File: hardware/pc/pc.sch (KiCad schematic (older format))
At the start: 126 parts, among them J1 Conn_Power, J2 Conn_PC, U1 74HC161, U10 74HC597, U11 74HC595, U12 74HC161, U13 74HC161, U14 74HC597, U15 74HC595, U16 74HC161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

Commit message: Added test points
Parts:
- added TP1: TestPoint, TestPoint:TestPoint_THTPad_D2.0mm_Drill1.0mm, symbol Connector:TestPoint
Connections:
- net GND: now also TP1.1

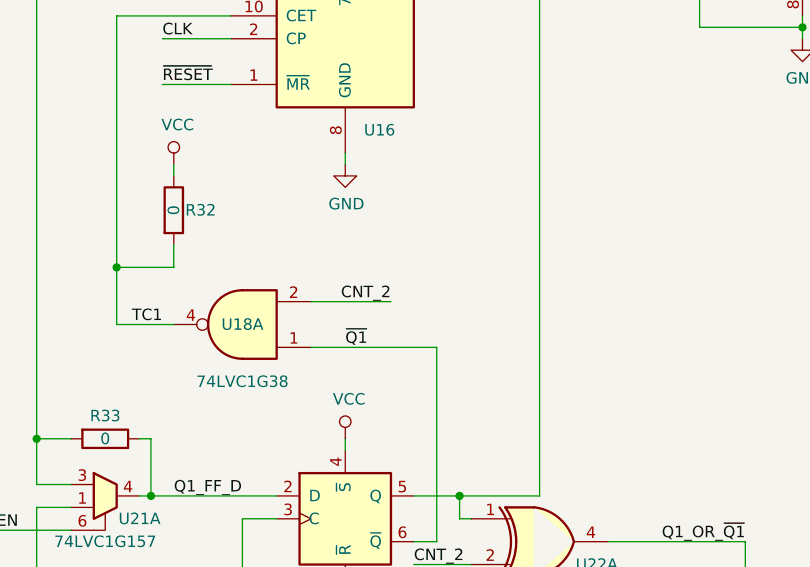
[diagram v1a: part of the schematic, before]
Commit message: Added errata to pc schematic
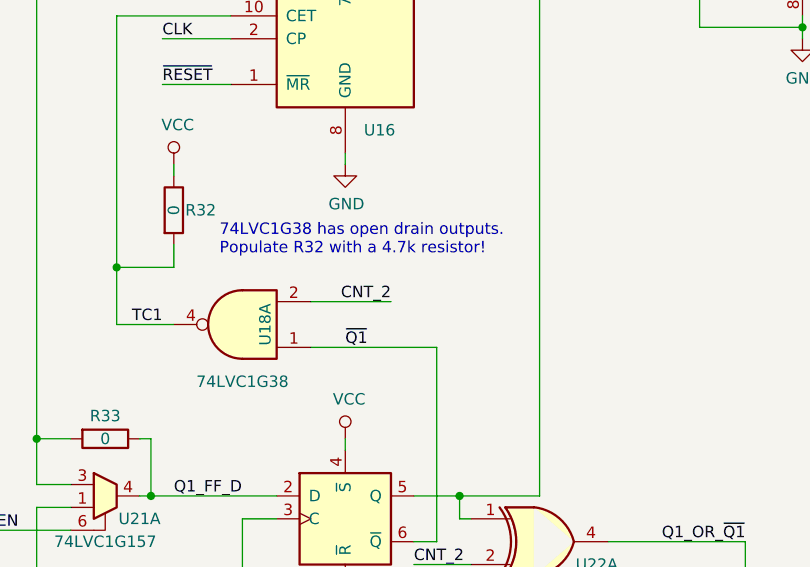
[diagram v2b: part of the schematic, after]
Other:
- note added: "74LVC1G38 has open drain outputs.\nPopulate R32 with a 4.7k resistor!"
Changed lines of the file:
@@
 EESchema Schematic File Version 4
-LIBS:pc-cache
-EELAYER 26 0
+EELAYER 30 0
 EELAYER END
 $Descr A2 16535 23386 portrait
@@
 U 1 1 5F0A6688
 P 6350 19550
-F 0 "U18" H 6350 19550 50  0000 C CNN
+F 0 "U18" V 6250 19550 50  0000 C CNN
 F 1 "74LVC1G38" H 6350 19800 50  0000 C CNN
 F 2 "Package_TO_SOT_SMD:SOT-23-5_HandSoldering" H 6350 19600 50  0001 C CNN
@@
 Wire Wire Line
 	11550 3050 11550 3150
+Text Notes 6250 19250 0    50   ~ 0
+74LVC1G38 has open drain outputs.\nPopulate R32 with a 4.7k resistor!
 $EndSCHEMATC

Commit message: Update all to Kicad 6
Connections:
- net CNT_~PE renamed CNT_~{PE}
- net OUT_S~P~ renamed OUT_S~{P}
- net Q1_OR_~Q1 renamed Q1_OR_~{Q1}
- net ~Q1 renamed ~{Q1}
- net ~RESET renamed ~{RESET}
